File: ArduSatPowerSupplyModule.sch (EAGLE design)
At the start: 81 parts, among them IC1 RT9276, IC2 LTC4054, IC3 ATMEGA32U4-QFN, Q1 2N7002, Q2 BSS138 N-MOSFET, Q3 MOSFET-PCHANNELSMT2, Q4 BSS138 N-MOSFET, SW1 SWITCH-DPDT, SW2 RESET, U1 MAX17043G+U, X3 USBSF-MICROB

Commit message: Completed routing
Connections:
- net +5V_SYS: no longer Q2.G, Q4.G, R10.2, R12.2
- net 5V_REG: now also Q2.G, Q4.G, R10.2, R12.2
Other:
- note removed: "Output Current Measurement"
- moved on the sheet: C1, C2, JP10, R1, R13, R2, R8, U1

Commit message: Linked I2C with CubeSat bus; clearance and overlay improvements
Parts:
- removed JP10: (no value), freetronics-master-v1:M02PTH
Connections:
- removed net H1L41: H1.41
- removed net H1L43: H1.43
- net MGMNT_SCL: now also H1.43; no longer JP10.1
- net MGMNT_SDA: now also H1.41; no longer JP10.2
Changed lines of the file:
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@@
 <part name="GND1" library="SparkFun" deviceset="GND" device=""/>
 <part name="GND20" library="freetronics" deviceset="GND" device=""/>
-<part name="JP10" library="freetronics-master-v1" deviceset="M02" device="PTH"/>
 </parts>
 <sheets>
@@
 <instance part="GND1" gate="1" x="25.4" y="312.42"/>
 <instance part="GND20" gate="1" x="40.64" y="254"/>
-<instance part="JP10" gate="G$1" x="180.34" y="464.82" rot="R180"/>
 </instances>
 <busses>
@@
 <wire x1="124.46" y1="25.4" x2="139.7" y2="25.4" width="0.1524" layer="91"/>
 <label x="127" y="25.4" size="1.778" layer="95"/>
-</segment>
-</net>
-<net name="H1L41" class="0">
-<segment>
-<pinref part="H1" gate="G$1" pin="41"/>
-<wire x1="124.46" y1="22.86" x2="139.7" y2="22.86" width="0.1524" layer="91"/>
-<label x="127" y="22.86" size="1.778" layer="95"/>
-</segment>
-</net>
-<net name="H1L43" class="0">
-<segment>
-<pinref part="H1" gate="G$1" pin="43"/>
-<wire x1="124.46" y1="20.32" x2="139.7" y2="20.32" width="0.1524" layer="91"/>
-<label x="127" y="20.32" size="1.778" layer="95"/>
 </segment>
 </net>
@@
 </segment>
 <segment>
-<pinref part="JP10" gate="G$1" pin="2"/>
-<wire x1="172.72" y1="462.28" x2="152.4" y2="462.28" width="0.1524" layer="91"/>
-<label x="154.94" y="462.28" size="1.778" layer="95"/>
+<pinref part="H1" gate="G$1" pin="41"/>
+<wire x1="124.46" y1="22.86" x2="139.7" y2="22.86" width="0.1524" layer="91"/>
+<label x="127" y="22.86" size="1.778" layer="95"/>
 </segment>
 </net>
@@
 </segment>
 <segment>
-<pinref part="JP10" gate="G$1" pin="1"/>
-<wire x1="172.72" y1="464.82" x2="152.4" y2="464.82" width="0.1524" layer="91"/>
-<label x="154.94" y="464.82" size="1.778" layer="95"/>
-</segment>
-</net>
+<pinref part="H1" gate="G$1" pin="43"/>
+<wire x1="124.46" y1="20.32" x2="139.7" y2="20.32" width="0.1524" layer="91"/>
+<label x="127" y="20.32" size="1.778" layer="95"/>
+</segment>
+</net>

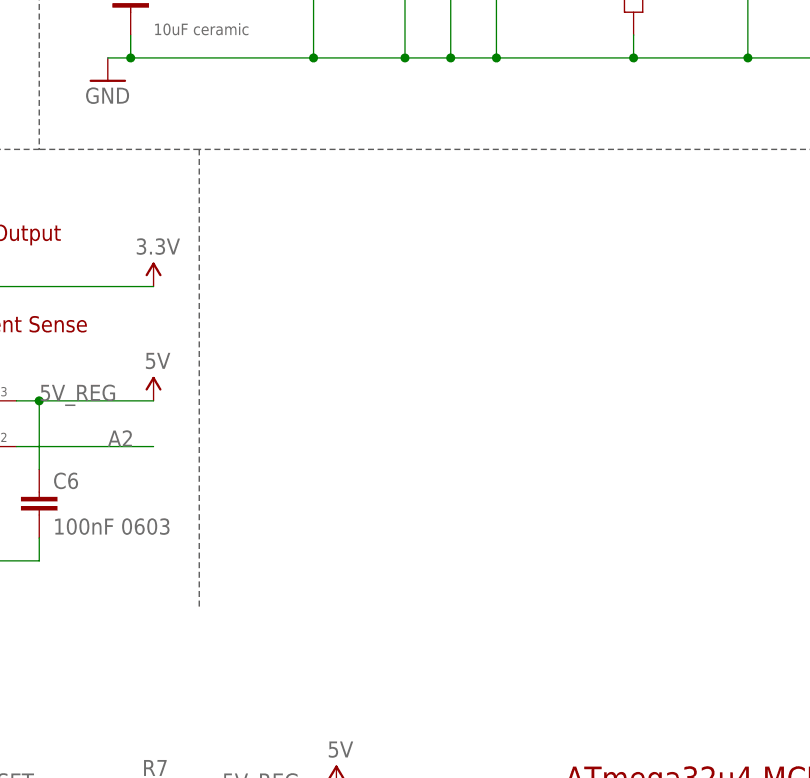
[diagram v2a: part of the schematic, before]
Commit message: Added optional I2C pull-ups on CubeSat bus side of the isolators. Changed polygon isolation to 0.012 on inner layers, 0.010 on outer. Improved spacing.
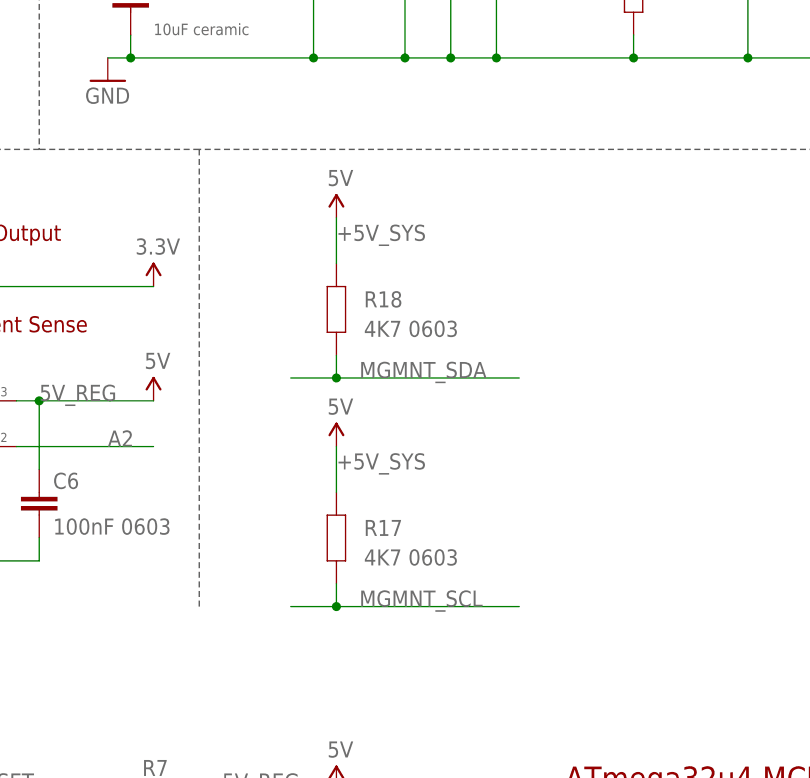
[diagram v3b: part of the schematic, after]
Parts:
- added R17, R18: 4K7 0603, freetronics-master-v1.1:RESISTOR0603
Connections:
- net +5V_SYS: now also R17.2, R18.2
- net MGMNT_SCL: now also R17.1
- net MGMNT_SDA: now also R18.1
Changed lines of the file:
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@@
 <part name="GND1" library="SparkFun" deviceset="GND" device=""/>
 <part name="GND20" library="freetronics" deviceset="GND" device=""/>
+<part name="R17" library="freetronics-master-v1.1" deviceset="RESISTOR" device="0603" value="4K7 0603"/>
+<part name="U$3" library="SparkFun" deviceset="5V" device=""/>
+<part name="R18" library="freetronics-master-v1.1" deviceset="RESISTOR" device="0603" value="4K7 0603"/>
+<part name="U$14" library="SparkFun" deviceset="5V" device=""/>
 </parts>
 <sheets>
@@
 <instance part="GND1" gate="1" x="25.4" y="312.42"/>
 <instance part="GND20" gate="1" x="40.64" y="254"/>
+<instance part="R17" gate="G$1" x="121.92" y="203.2" smashed="yes" rot="R90">
+<attribute name="NAME" x="124.968" y="203.4286" size="1.778" layer="95"/>
+<attribute name="VALUE" x="124.968" y="200.152" size="1.778" layer="96"/>
+</instance>
+<instance part="U$3" gate="G$1" x="121.92" y="213.36"/>
+<instance part="R18" gate="G$1" x="121.92" y="228.6" smashed="yes" rot="R90">
+<attribute name="NAME" x="124.968" y="228.8286" size="1.778" layer="95"/>
+<attribute name="VALUE" x="124.968" y="225.552" size="1.778" layer="96"/>
+</instance>
+<instance part="U$14" gate="G$1" x="121.92" y="238.76"/>
 </instances>
 <busses>
@@
 <label x="223.52" y="231.14" size="1.778" layer="95"/>
 <pinref part="U$18" gate="G$1" pin="5V"/>
+</segment>
+<segment>
+<pinref part="R18" gate="G$1" pin="2"/>
+<pinref part="U$14" gate="G$1" pin="5V"/>
+<wire x1="121.92" y1="233.68" x2="121.92" y2="238.76" width="0.1524" layer="91"/>
+<label x="121.92" y="236.22" size="1.778" layer="95"/>
+</segment>
+<segment>
+<pinref part="R17" gate="G$1" pin="2"/>
+<pinref part="U$3" gate="G$1" pin="5V"/>
+<wire x1="121.92" y1="208.28" x2="121.92" y2="213.36" width="0.1524" layer="91"/>
+<label x="121.92" y="210.82" size="1.778" layer="95"/>
 </segment>
 </net>
@@
 <label x="127" y="22.86" size="1.778" layer="95"/>
 </segment>
+<segment>
+<wire x1="142.24" y1="220.98" x2="121.92" y2="220.98" width="0.1524" layer="91"/>
+<pinref part="R18" gate="G$1" pin="1"/>
+<wire x1="121.92" y1="220.98" x2="116.84" y2="220.98" width="0.1524" layer="91"/>
+<wire x1="121.92" y1="223.52" x2="121.92" y2="220.98" width="0.1524" layer="91"/>
+<junction x="121.92" y="220.98"/>
+<label x="124.46" y="220.98" size="1.778" layer="95"/>
+</segment>
 </net>
 <net name="MGMNT_SCL" class="0">
@@
 <label x="127" y="20.32" size="1.778" layer="95"/>
 </segment>
-</net>
+<segment>
+<wire x1="142.24" y1="195.58" x2="121.92" y2="195.58" width="0.1524" layer="91"/>
+<pinref part="R17" gate="G$1" pin="1"/>
+<wire x1="121.92" y1="195.58" x2="116.84" y2="195.58" width="0.1524" layer="91"/>
+<wire x1="121.92" y1="198.12" x2="121.92" y2="195.58" width="0.1524" layer="91"/>
+<junction x="121.92" y="195.58"/>
+<label x="124.46" y="195.58" size="1.778" layer="95"/>
+</segment>
+</net>

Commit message: Added NanoSatisfi and ArduSat logos; clearances; DRC
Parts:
- removed B2: 2P-JST-PTH, freetronics-jon:FREETRONICS-LUKE_2P-JST-TH-RAPTH
- removed F2: 500mA PTC, freetronics-luke:PTC
- removed ICSP: ICSP, pinhead:PINHD-2X3
- removed JP9: I2C ADDR, freetronics-master-v1.1:PINHD-2X3
- removed LED6: Standby, freetronics-master-v1:LED0603
- removed R24: 3K3, freetronics-master-v1.1:RESISTOR0603
- removed R25: 10K, freetronics-master-v1.1:RESISTOR0603
- removed REG2: LD1117-SOT223, freetronics:V_REG_LM1117SOT223
- removed U$10, U$16, U$20: MAX4372, freetronics-jon:MAX4372
- removed U1: MAX17043G+U, SparkFun:MAX1704X
- removed X3: USBSF-MICROB, freetronics-jon:USBSF-MICROB
- added F1: 500mA PTC, freetronics-luke:PTC
- added IC10: ATMEGA32U4-QFN, freetronics-jon:ATMEGA32U4-QFN
- added IC4: LTC4054, freetronics-luke:LTC4054
- added IC5, IC7, IC9: MAX4372, freetronics-jon:MAX4372
- added IC6: RT9276, freetronics-luke:RT9276
- added IC8: LD1117-SOT223, freetronics:V_REG_LM1117SOT223
- added LED3: RGBLEDSMT, freetronics-master-v1:RGBLEDSMT
- added R19, R20: 10K 0603, freetronics-master-v1.1:RESISTOR0603
- added S1: USBSF-MICROB, freetronics-jon:USBSF-MICROB
- added S2, S4: (no value), freetronics-master-v1:M02PTH
- added S3: 2P-JST-PTH, freetronics-jon:FREETRONICS-LUKE_2P-JST-TH-RAPTH
- C1: value 10nF -> 1uF
- C10: value 10uF 6.3V A TANT -> 100nF 0603; device freetronics:CAP_POL1206 -> freetronics-master-v1.1:CAP0603
- C11: value 15pF 0603 -> 100nF 0603
- C12: value 15pF 0603 -> 1uF 0603
- C14, C15: value 100nF 0603 -> 15pF 0603
- C2: value 1uF -> 10nF
- C3: value 10uF ceramic -> 1uF; device freetronics-jon:C-EUC0805 -> freetronics:CAP0603
- C4: value 22uF -> 100nF 0603; device freetronics-jon:C-EUC1206K -> freetronics-master-v1.1:CAP0603
- C5: value 1uF -> 10uF ceramic; device freetronics:CAP0603 -> freetronics-jon:C-EUC0805
- C6: value 100nF 0603 -> 22uF; device freetronics-master-v1.1:CAP0603 -> freetronics-jon:C-EUC1206K
- C7: value 1uF 0603 -> 100nF 0603
- C8: value 100nF 0603 -> 1uF 0603; device freetronics-master-v1.1:CAP0603 -> freetronics-marc:CAP0603
- C9: value 1uF 0603 -> 10uF 6.3V A TANT; device freetronics-marc:CAP0603 -> freetronics:CAP_POL1206
- IC1: value RT9276 -> TMP102; device freetronics-luke:RT9276 -> freetronics-jon:TMP102
- IC2: value LTC4054 -> TMP102; device freetronics-luke:LTC4054 -> freetronics-jon:TMP102
- IC3: value ATMEGA32U4-QFN -> MAX17043G+U; device freetronics-jon:ATMEGA32U4-QFN -> SparkFun:MAX1704X
- JP5: value (none) -> ICSP; device freetronics-master-v1:M02PTH -> pinhead:PINHD-2X3
- JP6: value (none) -> I2C ADDR; device freetronics-master-v1:M02PTH -> freetronics-master-v1.1:PINHD-2X3
- LED1: value BLUE -> Charge; device SparkFun:LED0603 -> freetronics-master-v1:LED0603
- LED2: value JADEGREEN -> Standby; device SparkFun:LED0603 -> freetronics-master-v1:LED0603
- LED4: value RGBLEDSMT -> BLUE; device freetronics-master-v1:RGBLEDSMT -> SparkFun:LED0603
- LED5: value Charge -> JADEGREEN; device freetronics-master-v1:LED0603 -> SparkFun:LED0603
- Q2: value BSS138 N-MOSFET -> MOSFET-PCHANNELSMT2; device freetronics-master-v1:MOSFET-NCHANNELSMD -> freetronics-jon:MOSFET-PCHANNELSMT2
- Q3: value MOSFET-PCHANNELSMT2 -> BSS138 N-MOSFET; device freetronics-jon:MOSFET-PCHANNELSMT2 -> freetronics-master-v1:MOSFET-NCHANNELSMD
- R1: value 1k -> 1K
- R10: value 10K 0603 -> 33K
- R11: value 33K -> 180K
- R12: value 10K 0603 -> 20K0
- R13, R8: value 4.7k -> 0.15R 2010; device freetronics-master-v1.1:RESISTOR0603 -> freetronics-original:RESISTOR2010
- R15, R16: value 0.15R 2010 -> 4K7 0603; device freetronics-original:RESISTOR2010 -> freetronics-master-v1.1:RESISTOR0603
- R2: value 4.7k -> 4K7
- R21: value 1K -> 10K 0603
- R22: value 10K -> 2K2
- R23: value 10K -> 1K5
- R3: value 2K2 -> 3K3
- R4: value 1K5 -> 10K
- R5: value 180K -> 10K
- R6: value 20K0 -> 10K
- R7: value 10K 0603 -> 1K
- SW1: value SWITCH-DPDT -> SWITCH-DPDT2; device freetronics-jon:SWITCH-DPDT -> freetronics-jon:SWITCH-DPDT2
- renumbered RN3 to RN1, RN4 to RN2
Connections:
- removed net 3V3_REG: C1.1, JP2.2, JP8.11, R15.2, R4.1, U$10.RS-, U1.VDD
- removed net 5V_REG: C14.1, C15.1, C6.1, C9.1, IC3.AVCC, IC3.AVCC1, IC3.VCC, IC3.VCC1, ICSP.2, JP1.2, JP8.10, JP8.13, Q2.G, Q4.G, R10.2, R12.2, R13.2, R14.2, R3.1, R7.1, R8.2, REG2.IN, RN2A.1, RN2B.1, U$10.VCC, U$16.RS-, U$16.VCC, U$20.VCC
- removed net MGMNT_SCL: H1.43, Q4.D, R17.1
- removed net MGMNT_SDA: H1.41, Q2.D, R18.1
- new net 3.3V: C2.1, IC1.V+, IC2.ADD0, IC2.V+, IC3.VDD, IC9.RS-, JP4.2, JP8.11, R14.2, R23.1
- new net 5V: C10.1, C4.1, C7.1, C8.1, IC10.AVCC, IC10.AVCC1, IC10.VCC, IC10.VCC1, IC5.VCC, IC7.RS-, IC7.VCC, IC8.IN, IC9.VCC, JP3.2, JP5.2, JP8.10, JP8.13, Q3.G, Q4.G, R13.2, R17.2, R18.2, R19.1, R20.2, R21.2, R22.1, RN2A.1, RN2B.1
- new net SCL_SYS: H1.43, Q3.D, R16.1
- new net SDA_SYS: H1.41, Q4.D, R15.1
- net +5V_SYS: now also JP3.1, R15.2, R16.2; no longer JP1.1, R17.2, R18.2
- net 3V3: now also IC10.UCAP; no longer IC3.UCAP
- net A0: now also IC10.PF7(ADC7(TDI), IC5.OUT; no longer IC3.PF7(ADC7(TDI), U$20.OUT
- net A1: now also IC10.PF6(ADC6/TDO), IC7.OUT; no longer IC3.PF6(ADC6/TDO), U$16.OUT
- net A2: now also IC10.PF5(ADC5/TMS), IC9.OUT; no longer IC3.PF5(ADC5/TMS), U$10.OUT
- net A3: now also IC10.PF4(ADC4/TCK); no longer IC3.PF4(ADC4/TCK)
- net A4_SDA: now also IC10.PF1(ADC1), Q4.S, R21.1; no longer IC3.PF1(ADC1), Q2.S, R10.1
- net A5_SCL: now also IC10.PF0(ADC0), Q3.S, R20.1; no longer IC3.PF0(ADC0), Q4.S, R12.1
- net AREF: now also C11.1, IC10.AREF; no longer C8.1, IC3.AREF
- net CELL: now also C1.1, IC3.CELL; no longer C2.1, U1.CELL
- net D+: now also S1.D+; no longer X3.D+
- net D-: now also S1.D-; no longer X3.D-
- net D0: now also IC10.PD2(INT2/RXD1); no longer IC3.PD2(INT2/RXD1)
- net D1: now also IC10.PD3(INT3/TXD1); no longer IC3.PD3(INT3/TXD1)
- net D10_A11: now also IC10.PB6(OC1B/!OC4B!/ADC13), JP6.3; no longer IC3.PB6(OC1B/!OC4B!/ADC13), JP9.3
- net D11: now also IC10.PB7(OC0A/OC1C/RTS), JP6.1; no longer IC3.PB7(OC0A/OC1C/RTS), JP9.1
- net D12: now also IC10.PD6(T1/OC4D/ADC9); no longer IC3.PD6(T1/OC4D/ADC9)
- net D13: now also IC10.PC7(ICP3/CLK0/OC4A); no longer IC3.PC7(ICP3/CLK0/OC4A)
- net D2_SDA: now also IC10.PD1(INT1/SDA); no longer IC3.PD1(INT1/SDA)
- net D3_SCL: now also IC10.PD0(INT0/OC0B/SCL); no longer IC3.PD0(INT0/OC0B/SCL)
- net D4_A6: now also IC10.PD4(ICP1/ADC8); no longer IC3.PD4(ICP1/ADC8)
- net D5_SSDA: now also IC1.SDA, IC10.PC6(OC3A/!OC4A!), IC2.SDA, IC3.SDA, R17.1; no longer IC3.PC6(OC3A/!OC4A!), R8.1, U1.SDA
- net D6_A8_SSCL: now also IC1.SCL, IC10.PD7(OC4D/ADC10/T0), IC2.SCL, IC3.SCL, R18.1; no longer IC3.PD7(OC4D/ADC10/T0), R13.1, U1.SCL
- net D7_AIN0: now also IC10.PE6; no longer IC3.PE6
- net D8_A9: now also IC10.PB4(ADC11); no longer IC3.PB4(ADC11)
- net D9_A10: now also IC10.PB5(OC1A/!OC4B!/ADC12), JP6.5; no longer IC3.PB5(OC1A/!OC4B!/ADC12), JP9.5
- net FB: now also IC6.FB/NC, R11.2, R12.2; no longer IC1.FB/NC, R5.2, R6.2
- net GND: now also C10.2, C11.2, C12.2, C14.1, C15.1, C3.1, C5.2, C9.-, IC1.ADD0, IC10.GND, IC10.GND1, IC10.GND2, IC10.GND3, IC10.TGND, IC10.UGND, IC3.CTG, IC3.GND@4, IC3.GND@EP, IC4.GND, IC5.GND, IC6.EXP, IC6.GND, IC6.LBI, IC6.PGND, IC7.GND, IC8.ADJ, IC9.GND, JP1.1, JP5.6, JP6.2, JP6.4, JP6.6, LED3.C-B, LED4.C, LED5.C, R12.1, R3.2, R4.2, R5.2, S1.FIX1, S1.FIX2, S1.GND, S1.TAB1, S1.TAB2, S2.1, S3.NEG, S4.2; no longer B2.NEG, C10.-, C11.1, C12.1, C14.2, C15.2, C3.2, C5.1, C9.2, IC1.EXP, IC1.LBI, IC1.PGND, IC3.GND, IC3.GND1, IC3.GND2, IC3.GND3, IC3.TGND, IC3.UGND, ICSP.6, JP4.1, JP5.2, JP6.1, JP9.2, JP9.4, JP9.6, LED1.C, LED2.C, LED4.C-B, R23.2, R24.2, R25.2, R6.1, REG2.ADJ, U$10.GND, U$16.GND, U$20.GND, U1.CTG, U1.GND@4, U1.GND@EP, X3.FIX1, X3.FIX2, X3.GND, X3.TAB1, X3.TAB2
- net LX: now also IC6.LX; no longer IC1.LX
- net MISO: now also IC10.PB3(PDO/MISO), JP5.1; no longer IC3.PB3(PDO/MISO), ICSP.1
- net MOSI: now also IC10.PB2(PDI/MOSI), JP5.4; no longer IC3.PB2(PDI/MOSI), ICSP.4
- net N$1: now also LED5.A, R23.2; no longer LED2.A, R4.2
- net N$10: now also IC10.PE2(HWB); no longer IC3.PE2(HWB)
- net N$11: now also C14.2, IC10.XTAL1; no longer C11.2, IC3.XTAL1
- net N$12: now also C15.2, IC10.XTAL2; no longer C12.2, IC3.XTAL2
- net N$14: now also LED3.A-B; no longer LED4.A-B
- net N$15: now also C6.1, IC6.VOUT, IC7.RS+, R11.1, R13.1; no longer C4.1, IC1.VOUT, R14.1, R5.1, U$16.RS+
- net N$16: now also LED3.A-R; no longer LED4.A-R
- net N$17: now also LED3.A-G; no longer LED4.A-G
- net N$2: now also JP1.2, JP2.1; no longer JP3.1, JP4.2
- net N$20: now also IC4.BAT, IC5.RS+, R8.1; no longer IC2.BAT, R16.1, U$20.RS+
- net N$235: now also LED2.C; no longer LED6.C
- net N$248: now also LED1.A, LED2.A, R7.2; no longer LED5.A, LED6.A, R21.2
- net N$249: now also F1.P$1, S1.VBUS; no longer F2.P$1, X3.VBUS
- net N$251: now also IC4.!CHRG, LED1.C, R6.2; no longer IC2.!CHRG, LED5.C, R22.2
- net N$252: now also IC4.PROG, R5.1; no longer IC2.PROG, R23.1
- net N$299: now also R3.1; no longer R24.1
- net N$3: now also C9.+, IC8.OUT, IC8.OUT@1, IC9.RS+, R14.1; no longer C10.+, R15.1, REG2.OUT, REG2.OUT@1, U$10.RS+
- net N$310: now also R4.1; no longer R25.1
- net N$4: now also JP2.2; no longer JP3.2
- net N$5: now also Q2.S, R10.1; no longer Q3.S, R11.1
- net N$6: now also LED4.A, R22.2; no longer LED1.A, R3.2
- net N$7: now also Q2.G, R10.2; no longer Q3.G, R11.2
- net PWR: now also C5.1, IC6.EN, IC6.VBAT, Q2.D; no longer C3.1, IC1.EN, IC1.VBAT, Q3.D
- net QST: now also IC3.QST; no longer U1.QST
- net RD+: now also IC10.D+; no longer IC3.D+
- net RD-: now also IC10.D-; no longer IC3.D-
- net RESET: now also IC10./RESET, JP5.5, R19.2; no longer IC3./RESET, ICSP.5, R7.2
- net RXLED_SS: now also IC10.PB0(SS), LED3.C-G; no longer IC3.PB0(SS), LED4.C-G
- net SCK: now also IC10.PB1(SCK), JP5.3; no longer IC3.PB1(SCK), ICSP.3
- net TX_LED: now also IC10.PD5(XCK/CTS), LED3.C-R; no longer IC3.PD5(XCK/CTS), LED4.C-R
- net USBVCC: now also C12.1, C3.2, F1.P$2, IC10.UVCC, IC10.VBUS, IC4.VCC, R6.1, R7.1, S2.2; no longer C5.2, C7.1, F2.P$2, IC2.VCC, IC3.UVCC, IC3.VBUS, JP6.2, R21.1, R22.1
- net VBAT: now also IC5.RS-, R8.2, S3.POS, S4.1; no longer B2.POS, JP5.1, R16.2, U$20.RS-
- net VCC_SYS: now also JP4.1; no longer JP2.1
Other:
- note added: "(Not fitted)"
- note added: "Addr: 72 (0x48)"
- note added: "Addr: 73 (0x49)"
- note added: "Bottom Temperature Sensor"
- note added: "Connect across SJ1, SJ2, SJ3 after other routing"
- note added: "Local I2C Pullups"
- note added: "SJ1"
- note added: "SJ2"
- note added: "System I2C Pullups"
- note added: "Top Temperature Sensor"
- note added: "V1.0 (2012-12-25)"
- note removed: "Connect across HWB after other routing"
- note removed: "S1"
- note removed: "S2"
- note removed: "V1.0 (2011-12-16)"
- moved on the sheet: C1, C11, C12, C14, C15, C2, C3, C4, C5, C6, C7, C8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

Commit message: Moved 3.3V power supply input to before the 5V current sense resistor
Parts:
- added SJ4, SJ5: VBATT45, freetronics-master-v1:SJTINY
- IC6: value RT9276 -> RT9276-50
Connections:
- removed net H2L45: H2.45
- removed net H2R46: H2.46
- removed net N$15: C6.1, IC6.VOUT, IC7.RS+, R11.1, R13.1
- removed net VBAT: IC5.RS-, R1.2, R8.2, S3.POS, S4.1, SW1.2, SW1.5
- new net 5VRAW: C6.1, C8.1, IC6.VOUT, IC7.RS+, IC8.IN, R11.1, R13.1
- new net VBATT: IC5.RS-, R1.2, R8.2, S3.POS, S4.1, SJ4.1, SJ5.1, SW1.2, SW1.5
- new net VBATT45: H2.45, SJ4.2
- new net VBATT46: H2.46, SJ5.2
- net 5V: no longer C8.1, IC8.IN
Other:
- note added: "No need to place R11 & R12. Pads provided for compatibility with variable-output versions of the RT9276. No harm placing though."
- note added: "at 2.3A max."
- note removed: "at 500mA max."
- moved on the sheet: C10, C8, C9, IC8, IC9, R14, R15, R16, R17, R18

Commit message: Routing, DRC, overlay
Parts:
- removed F1: 500mA PTC, freetronics-luke:PTC
- removed IC1, IC2: TMP102, freetronics-jon:TMP102
- removed IC4: LTC4054, freetronics-luke:LTC4054
- removed IC5, IC9: MAX4372, freetronics-jon:MAX4372
- removed IC6: RT9276-50, freetronics-luke:RT9276
- removed IC8: LD1117-SOT223, freetronics:V_REG_LM1117SOT223
- removed JP3, JP4: (no value), freetronics-master-v1:M02PTH
- removed JP6: I2C ADDR, freetronics-master-v1.1:PINHD-2X3
- removed RN1: 22R, resistor-dil:4R-NCAY16
- removed S3: 2P-JST-PTH, freetronics-jon:FREETRONICS-LUKE_2P-JST-TH-RAPTH
- added C16, C22: 10nF, freetronics-jon:C-EU0402C
- added C17, C23: 100uF, freetronics-jon:C-EUC1206K
- added C18, C27: 47uF, freetronics-jon:C-EUC1206K
- added C19, C25: 1nF, freetronics-jon:C-EU0402C
- added C20, C26: 100pF, freetronics-jon:C-EU0402C
- added C21: 100nF 0603, freetronics-jon:C-EU0402C
- added C24: 27pF 0603, freetronics-master-v1.1:CAP0603
- added C28: 82pF 0603, freetronics-master-v1.1:CAP0603
- added C29: 330uF 6.3V Sanyo TPB D3L, freetronics-jon:CAP_POLD3L
- added C61, C62: 100nF 0402, freetronics-jon:C-EU0402C
- added IC11: MAX4372F, freetronics-jon:MAX4372
- added IC18, IC19: TMP102, freetronics-jon:TMP102
- added J1: POWER_JACKPTH, freetronics-master-v1:POWER_JACKPTH
- added L2, L3: 4.7uH, freetronics-luke:INDUCTOR
- added MNT1, MNT2, MNT3, MNT4: HOLE3.2MM, freetronics-jon:HOLE3.2MM
- added Q43, Q44, Q45, Q46, Q5: RJU003N03 N-MOSFET, freetronics-jon:MOSFET-NSOT-323
- added R24, R30: 49.9K, freetronics-jon:RESISTOR0402
- added R25: 187K, freetronics-jon:RESISTOR0402
- added R26, R32: 100K, freetronics-jon:RESISTOR0402
- added R27, R33: 845K, freetronics-jon:RESISTOR0402
- added R28, R34: 15K, freetronics-jon:RESISTOR0402
- added R29: 0.1R 2010, freetronics-original:RESISTOR2010
- added R31: 115K, freetronics-jon:RESISTOR0402
- added R35: 1M 1% 0603, freetronics-master-v1.1:RESISTOR0603
- added R36: 93.1K 1% 0603, freetronics-master-v1.1:RESISTOR0603
- added R37: 249K 1% 0603, freetronics-master-v1.1:RESISTOR0603
- added R38, R39: 22R, freetronics-jon:RESISTOR0402
- added R83, R84, R85, R86: 10K 0402, freetronics-jon:RESISTOR0402
- added U$10: CELLHOLDER2, freetronics-jon:CELLHOLDER2
- added U$11: LTC3115, freetronics-jon:LTC3115
- added U$12, U$15: LTC3536, freetronics-jon:LTC3536
- added U$19: LTC4078, freetronics-jon:LTC4078
- added Z4: 50V 1W Zener, freetronics-master-v1:DIODESMA
- C10: value 100nF 0603 -> 3300pF 0603
- C3: value 1uF -> 4.7uF TANTALUM; device freetronics:CAP0603 -> freetronics-jon:C-EUC1206K
- C4: value 100nF 0603 -> 1uF TANTALUM; device freetronics-master-v1.1:CAP0603 -> freetronics-jon:C-EUC1206K
- C5: value 10uF ceramic -> 1uF TANTALUM; device freetronics-jon:C-EUC0805 -> freetronics-jon:C-EUC1206K
- C6: value 22uF -> 100nF 0603; device freetronics-jon:C-EUC1206K -> freetronics-master-v1.1:CAP0603
- C7: device freetronics-master-v1.1:CAP0603 -> freetronics-jon:C-EU0402C
- C8: value 1uF 0603 -> 100nF 0603; device freetronics-marc:CAP0603 -> freetronics-master-v1.1:CAP0603
- C9: value 10uF 6.3V A TANT -> 10uF Murata GRM55DR61H106K 2220; device freetronics:CAP_POL1206 -> freetronics-jon:C-EUC2220K
- IC7: value MAX4372 -> MAX4372F
- L1: value 7.4uH -> 33uH Coilcraft MSS1260-333ML; device freetronics-luke:INDUCTOR -> freetronics-jon:INDUCTOR
- LED1: value Charge -> RED 0603
- LED2: value Standby -> BLUE 0603
- LED4, LED5: device SparkFun:LED0603 -> freetronics-master-v1:LED0603
- Q1: value 2N7002 -> RJU003N03 N-MOSFET; device freetronics-luke:2N7002 -> freetronics-jon:MOSFET-NSOT-323
- Q3, Q4: device freetronics-master-v1:MOSFET-NCHANNELSMD -> freetronics-jon:MOSFET-NSOT-323
- R11: value 180K -> 1K
- R12: value 20K0 -> 121K 1% 0603
- R13: value 0.15R 2010 -> 0.1R 2010
- R14: value 0.15R 2010 -> 249K 1% 0603; device freetronics-original:RESISTOR2010 -> freetronics-master-v1.1:RESISTOR0603
- R17, R18: value 4K7 0603 -> 10K 0402; device freetronics-master-v1.1:RESISTOR0603 -> freetronics-jon:RESISTOR0402
- R20, R21: device freetronics-master-v1.1:RESISTOR0603 -> freetronics-jon:RESISTOR0402
- R23: value 1K5 -> 1K
- R3: value 3K3 -> 2K2
- R4: value 10K -> 1K 1% 0603
- R5: value 10K -> 1.05K 1% 0603
- R6: value 10K -> 1.18K 1% 0603
- R8: value 0.15R 2010 -> 10K 0603; device freetronics-original:RESISTOR2010 -> freetronics-master-v1.1:RESISTOR0603
- SJ1: value SJ -> VBATT45; device freetronics-luke:SJ -> freetronics-master-v1:SJTINY
- SJ2: value SJ -> VBATT46; device freetronics-luke:SJ -> freetronics-master-v1:SJTINY
- SJ4: value VBATT45 -> 5V_EN
- SJ5: value VBATT45 -> 3V3_EN
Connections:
- net D0 renamed D0_RX
- net D1 renamed D1_TX
- removed net 5VRAW: C6.1, C8.1, IC6.VOUT, IC7.RS+, IC8.IN, R11.1, R13.1
- removed net A4_SDA: IC10.PF1(ADC1), JP8.2, Q4.S, R21.1
- removed net A5_SCL: IC10.PF0(ADC0), JP8.1, Q3.S, R20.1
- removed net D5_SSDA: IC1.SDA, IC10.PC6(OC3A/!OC4A!), IC2.SDA, IC3.SDA, JP7.6, R17.1
- removed net D6_A8_SSCL: IC1.SCL, IC10.PD7(OC4D/ADC10/T0), IC2.SCL, IC3.SCL, JP7.7, R18.1
- removed net FB: IC6.FB/NC, R11.2, R12.2
- removed net LX: IC6.LX, L1.2
- removed net N$235: LED2.C, Q1.D
- removed net N$249: F1.P$1, S1.VBUS
- removed net N$252: IC4.PROG, R5.1, SJ1.2, SJ2.2
- removed net N$299: R3.1, SJ1.1
- removed net N$310: R4.1, SJ2.1
- removed net PWR: C5.1, IC6.EN, IC6.VBAT, L1.1, Q2.D
- removed net SCL_SYS: H1.43, Q3.D, R16.1
- removed net SDA_SYS: H1.41, Q4.D, R15.1
- new net 3V3SENSED: C16.1, C7.1, IC7.RS-, IC7.VCC, R13.2, U$12./SHDN, U$12.VIN
- new net 5VSENSED: C21.1, C22.1, IC11.RS-, IC11.VCC, R29.2, U$15./SHDN, U$15.VIN
- new net A4: IC10.PF1(ADC1), JP8.2
- new net A5: IC10.PF0(ADC0), JP8.1
- new net BAT: R1.2, R3.1, R7.1, S4.1, SW1.2, SW1.5, U$19.BAT
- new net D5: IC10.PC6(OC3A/!OC4A!), JP7.6
- new net D6_A8: IC10.PD7(OC4D/ADC10/T0), JP7.7
- new net N$10001: IC18.SDA, Q44.S, R84.1
- new net N$10002: IC19.SDA, Q46.S, R86.1
- new net N$10003: IC19.SCL, Q45.S, R85.1
- new net N$15: R24.1, U$12.VC
- new net N$18: L2.1, U$12.SW1
- new net N$19: L2.2, U$12.SW2
- new net N$21: R26.1, U$12.RT
- new net N$22: L3.1, U$15.SW1
- new net N$23: C19.1, R24.2
- new net N$25: C20.2, R28.1
- new net N$26: C19.2, C20.1, R25.1, R27.1, U$12.FB
- new net N$27: LED2.C, U$19./PWR
- new net N$28: L3.2, U$15.SW2
- new net N$29: R32.1, U$15.RT
- new net N$30: C25.1, R30.2
- new net N$31: R30.1, U$15.VC
- new net N$32: C26.2, R34.1
- new net N$33: C25.2, C26.1, R31.1, R33.1, U$15.FB
- new net N$35: R4.1, U$19.ITERM
- new net N$36: R11.2, U$19.ENABLE
- new net N$37: C10.1, R36.2
- new net N$39: C3.2, U$11.PVCC, U$11.PWM/SYNC, U$11.VCC, Z4.C
- new net N$40: C6.2, U$11.BST1
- new net N$41: C8.2, U$11.BST2
- new net N$42: C6.1, L1.1, U$11.SW1
- new net N$43: C8.1, L1.2, U$11.SW2
- new net N$44: C24.1, R36.1, U$11.VC
- new net N$45: C10.2, C24.2, R14.2, R35.1, R37.1, U$11.FB
- new net N$47: R12.2, U$11.RT
- new net N$49: C28.2, R37.2
- new net N$8: IC3.SDA, Q1.S, R17.1
- new net N$9: IC3.SCL, Q5.S, R18.1
- new net N$9999: IC18.SCL, Q43.S, R83.1
- new net PVIN: C9.2, J1.PWR, S2.2, U$11.PVIN, U$11.RUN, U$11.VIN
- new net PVOUT: C28.1, C29.+, C5.2, R35.2, U$11.PVOUT, U$19.DCIN, Z4.A
- new net SCL: H1.43, Q3.D, Q43.D, Q45.D, Q5.D, R16.1
- new net SDA: H1.41, Q1.D, Q4.D, Q44.D, Q46.D, R15.1
- net +5V_SYS: now also SJ4.2; no longer JP3.1
- net 3.3V: now also C17.2, C27.2, C61.1, C62.1, IC18.V+, IC19.ADD0, IC19.V+, Q1.G, Q43.G, Q44.G, Q45.G, Q46.G, Q5.G, R17.2, R18.2, R27.2, R28.2, R83.2, R84.2, R85.2, R86.2, SJ5.1, U$12.VOUT; no longer IC1.V+, IC2.ADD0, IC2.V+, IC9.RS-, JP4.2, R14.2
- net 5V: now also C18.2, C23.2, R33.2, R34.2, SJ4.1, U$15.VOUT; no longer C10.1, C4.1, C7.1, IC5.VCC, IC7.RS-, IC7.VCC, IC9.VCC, JP3.2, R13.2, R17.2, R18.2
- net A0: now also R5.1, U$19.IDC; no longer IC5.OUT
- net A1: now also R6.1, U$19.IUSB; no longer IC7.OUT
- net A2: now also IC11.OUT; no longer IC9.OUT
- net A3: now also IC7.OUT
- net D+: now also R39.1; no longer RN1A.2
- net D-: now also R38.1; no longer RN1D.2
- net D10_A11: no longer JP6.3
- net D11: no longer JP6.1
- net D2_SDA: now also Q4.S, R21.1
- net D3_SCL: now also Q3.S, R20.1
- net D9_A10: no longer JP6.5
- net GND: now also C16.2, C17.1, C18.1, C21.2, C22.2, C23.1, C27.1, C29.-, C4.1, C5.1, C61.2, C62.2, C9.1, IC11.GND, IC18.ADD0, IC18.GND, IC19.GND, J1.GND, J1.GNDBREAK, MNT1.P$1, MNT2.P$1, MNT3.P$1, MNT4.P$1, R14.1, R25.2, R26.2, R31.2, R32.2, R6.2, R8.2, U$11.GND1, U$11.GND2, U$11.PGND, U$12.MODE/SYNC, U$12.SGND, U$12.TGND, U$15.MODE/SYNC, U$15.SGND, U$15.TGND, U$19.GND; no longer C10.2, C4.2, C5.2, C6.2, C8.2, C9.-, IC1.ADD0, IC1.GND, IC2.GND, IC4.GND, IC5.GND, IC6.EXP, IC6.GND, IC6.LBI, IC6.PGND, IC8.ADJ, IC9.GND, JP6.2, JP6.4, JP6.6, Q1.S, R3.2, S3.NEG
- net N$20: now also U$19.BATDET; no longer IC4.BAT, IC5.RS+
- net N$248: no longer LED2.A
- net N$251: now also U$19./CHRG; no longer IC4.!CHRG, Q1.G, R6.2
- net N$3: now also LED2.A, R3.2; no longer C9.+, IC8.OUT, IC8.OUT@1, IC9.RS+, R14.1
- net RD+: now also R39.2; no longer RN1A.1
- net RD-: now also R38.2; no longer RN1D.1
- net USBVCC: now also C4.2, R11.1, S1.VBUS, U$19.USBIN; no longer C3.2, F1.P$2, IC4.VCC, R6.1, R7.1, S2.2
- net VBATT: now also IC11.RS+, IC7.RS+, Q2.D, R13.1, R29.1, SJ1.1, SJ2.1; no longer IC5.RS-, R1.2, R8.2, S3.POS, S4.1, SJ4.1, SJ5.1, SW1.2, SW1.5
- net VBATT45: now also SJ1.2; no longer SJ4.2
- net VBATT46: now also SJ2.2; no longer SJ5.2
- net VCC_SYS: now also SJ5.2; no longer JP4.1
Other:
- note added: "(C)2013 Freetronics Pty Ltd: www.freetronics.com"
- note added: "1A max if VIN > 3.6V 2A max if VIN > 6V"
- note added: "300mA for VIN >= 1.8V 1A for VIN >= 3V"
- note added: "3V3 Link To CubeSat Bus"
- note added: "3V3 Out Current Sense"
- note added: "3V3 Voltage Regulator"
- note added: "5V In"
- note added: "5V Link To CubeSat Bus"
- note added: "5V Out Current Sense"
- note added: "5V Voltage Regulator"
- note added: "950mA max charge on DCIN 850mA max charge on USBIN"
- note added: "Battery Fuel Gauge"
- note added: "CHRG LED blinks when battery not present Charge current sense is calculated by I = (VIUSB / RIUSB) * 1000 Begins charge cycle when VBAT falls below 4.1V (ie: 80-90% capacity) to keep battery close to charged"
- note added: "Coilcraft XFL4020"
- note added: "Connect across SJ3 after other routing"
- note added: "DC Input: 2.7-40Vdc"
- note added: "DC in current sense"
- note added: "Flying Lead Battery Connector"
- note added: "Grounded Mounting Holes"
- note added: "I2C Addr: 72 (0x48)"
- note added: "I2C Addr: 73 (0x49)"
- note added: "LiPo Charger (2 x 5V Inputs)"
- note added: "Output: 5Vdc"
- note added: "PV In Current Sense"
- note added: "Short across SJ4 after other routing"
- note added: "Short across SJ5 after other routing"
- note added: "USB In Current Sense"
- note added: "USB Input: 5Vdc <=850mA"
- note added: "USB in current sense"
- note added: "V1.0 (2013-01-14)"
- note added: "VBATT Links To CubeSat Bus"
- note removed: "(C)2012 Freetronics Pty Ltd: www.freetronics.com"
- note removed: "0603"
- note removed: "1%"
- note removed: "100 mA"
- note removed: "10V"
- note removed: "1812"
- note removed: "200 mA"
- note removed: "2mm JST Li-Poly Battery Connector"
- note removed: "3V3"
- note removed: "3V3 Power Supply (Linear Reg)"
- note removed: "403 mA"
- note removed: "503 mA"
- note removed: "5V"
- note removed: "5V Power Supply (Voltage Boost Converter)"
- note removed: "800mA"
- note removed: "Addr: 72 (0x48)"
- note removed: "Addr: 73 (0x49)"
- note removed: "Alternate Battery Connector"
- note removed: "Alternate Input"
- note removed: "Battery State Measurement"
- note removed: "C4: 1206 ceramic"
- note removed: "CDRH"
- note removed: "Charge Current Configuration"
- note removed: "Charge Current Sense"
- note removed: "Charge current"
- note removed: "Closed"
- note removed: "Connect across SJ1, SJ2, SJ3 after other routing"
- note removed: "Green"
- note removed: "I2C Address: A0 = D9 A1 = D10 A2 = D11"
- note removed: "Input: 5Vdc 500mA"
- note removed: "L1: Same inductor as EtherMega"
- note removed: "LiPo Charger (5V Input)"
- note removed: "Local I2C Pullups"
- note removed: "No need to place R11 & R12. Pads provided for compatibility with variable-output versions of the RT9276. No harm placing though."
- note removed: "Open"
- note removed: "Output Isolation"
- note removed: "Red"
- note removed: "S-I2C"
- note removed: "SJ1"
- note removed: "SJ2"
- note removed: "SOT-23"
- note removed: "V1.0 (2012-12-25)"
- note removed: "Vout = 5.0V"
- note removed: "at 2.3A max."
- note removed: "https://www.sparkfun.com/products/8483 https://www.sparkfun.com/products/8484"
